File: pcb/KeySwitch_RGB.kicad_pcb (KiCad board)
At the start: 2 copper layers, 3.4 x 3 mm, 6 parts, among them K1 SW_Push

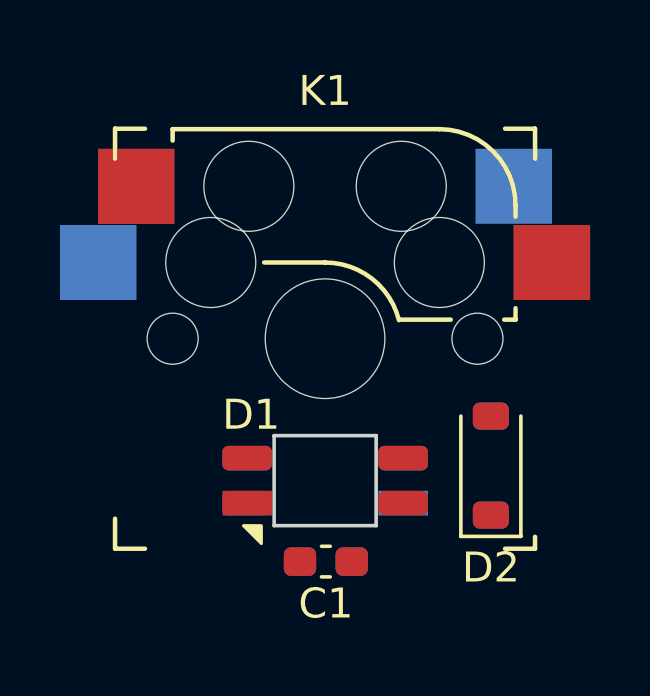
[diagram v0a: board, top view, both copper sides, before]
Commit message: Renumbering all reference designations and adding an initial layout for each keyswtich sub-pcb.
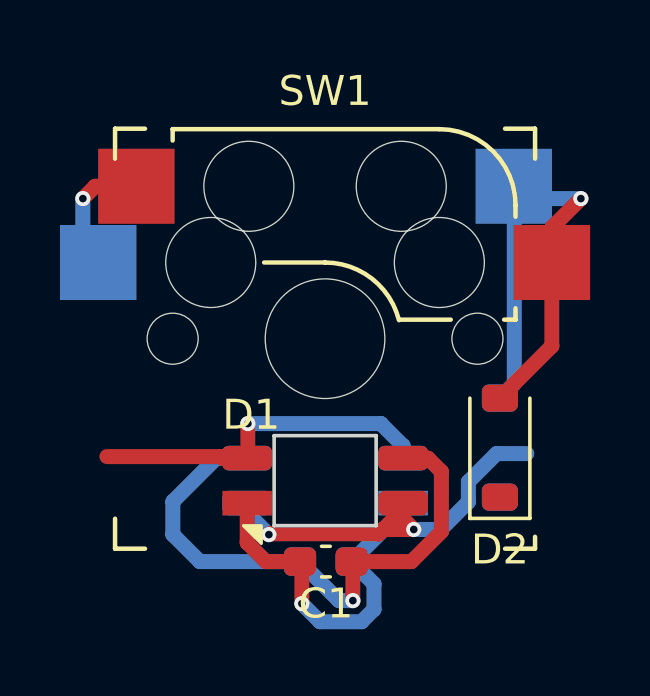
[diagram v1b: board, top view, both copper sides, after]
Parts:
- SW1: renamed from K1; value SW_Push -> CPG151101S11
- moved D2 0.67 mm to (110.5, 66.9)
- moved D3 0.67 mm to (110.5, 66.9)
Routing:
- net VSYS: track 0.00 -> 19.3 mm, vias 0 -> 1
- net Net-(D2-A): track 0.00 -> 17.4 mm, vias 0 -> 1
- net /LED_Out: track 0.00 -> 13.8 mm, vias 0 -> 2
- net GND: track 0.00 -> 12.2 mm, vias 0 -> 1
- net /LED_In: track 0.00 -> 11.8 mm, vias 0 -> 1
- net /Col: track 0.00 -> 4.29 mm, vias 0 -> 1
